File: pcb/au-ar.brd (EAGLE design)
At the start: 65 x 45 mm, 44 parts, among them U1 TPD12S520DBTR, U2 TPD12S521DBTR

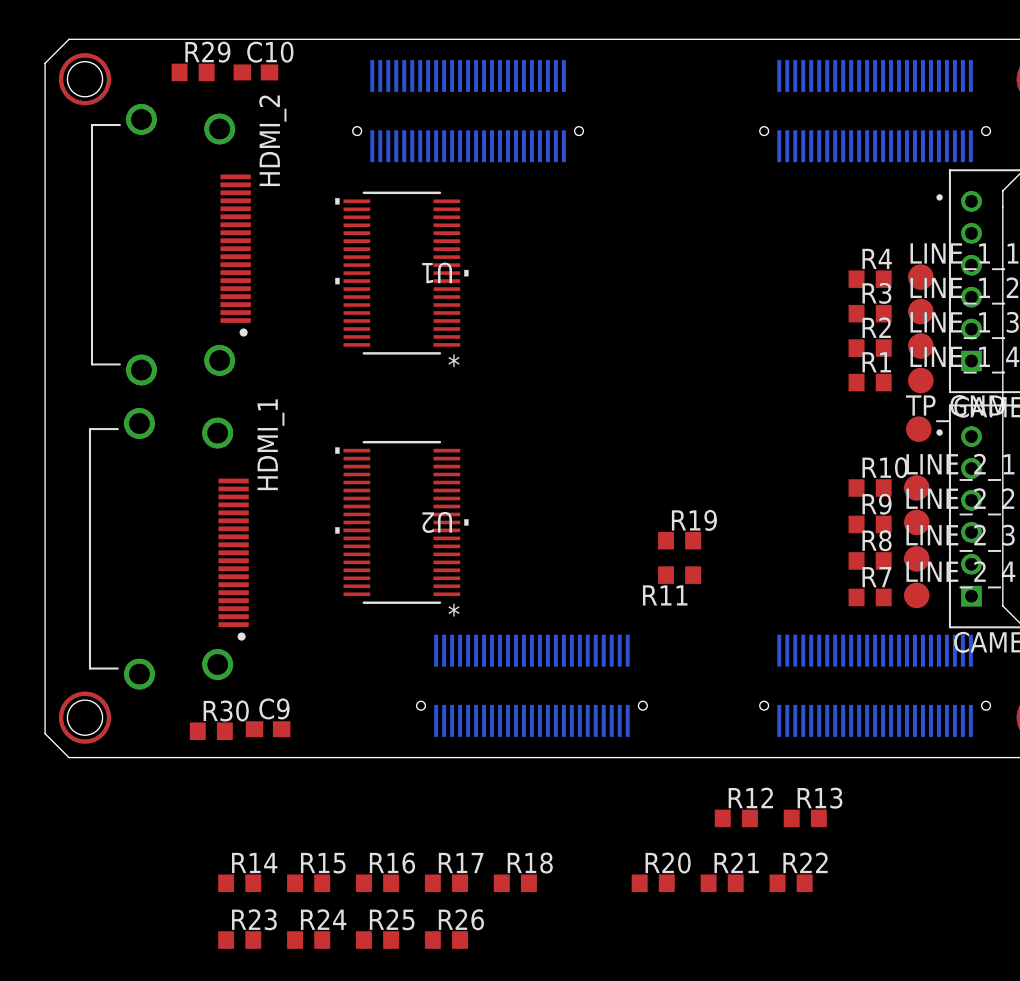
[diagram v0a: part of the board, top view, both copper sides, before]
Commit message: placed signal config resistors for camera trigger interface. relocated hdmi ports
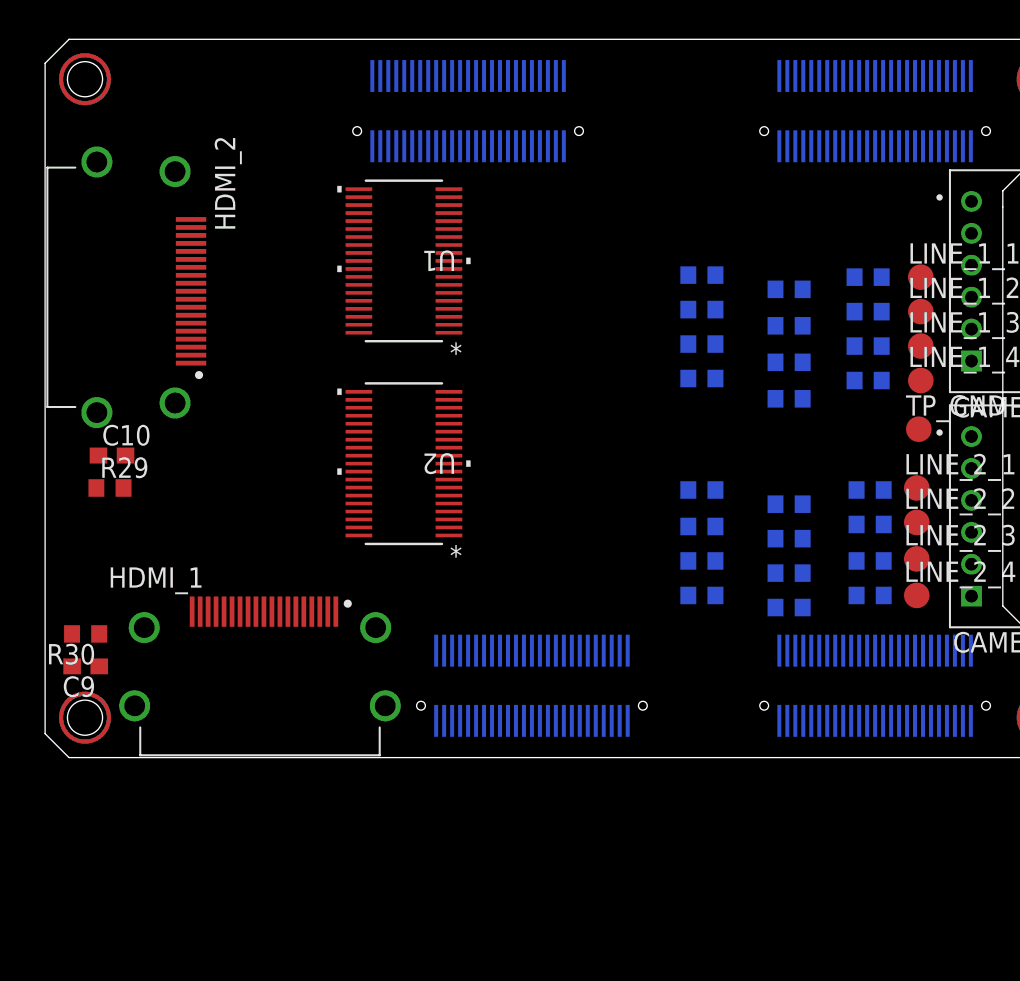
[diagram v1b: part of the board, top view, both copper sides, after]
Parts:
- moved R14 50.7 mm to (46.6, 29.3), flipped to the bottom
- moved R22 38.5 mm to (41.1, 30.2), flipped to the bottom, turned to 180 degrees
- moved R23 36.1 mm to (41.1, 10.2), flipped to the bottom, turned to 180 degrees
- moved R21 36.0 mm to (41.1, 28.1), flipped to the bottom, turned to 180 degrees
- moved R15 34.7 mm to (46.6, 9.40), flipped to the bottom
- moved R24 34.2 mm to (41.1, 12.3), flipped to the bottom, turned to 180 degrees
- moved R20 33.9 mm to (41.1, 25.9), flipped to the bottom, turned to 180 degrees
- moved R25 32.9 mm to (41.1, 14.5), flipped to the bottom, turned to 180 degrees
- moved R26 32.4 mm to (41.1, 16.8), flipped to the bottom, turned to 180 degrees
- moved R16 32.3 mm to (46.6, 11.6), flipped to the bottom
- moved R13 30.9 mm to (46.6, 27.1), flipped to the bottom
- moved R17 30.4 mm to (46.6, 13.7), flipped to the bottom
- moved R18 29.3 mm to (46.6, 15.9), flipped to the bottom
- moved R12 28.8 mm to (46.6, 24.8), flipped to the bottom
- moved R29 26.6 mm to (4.06, 16.9)
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
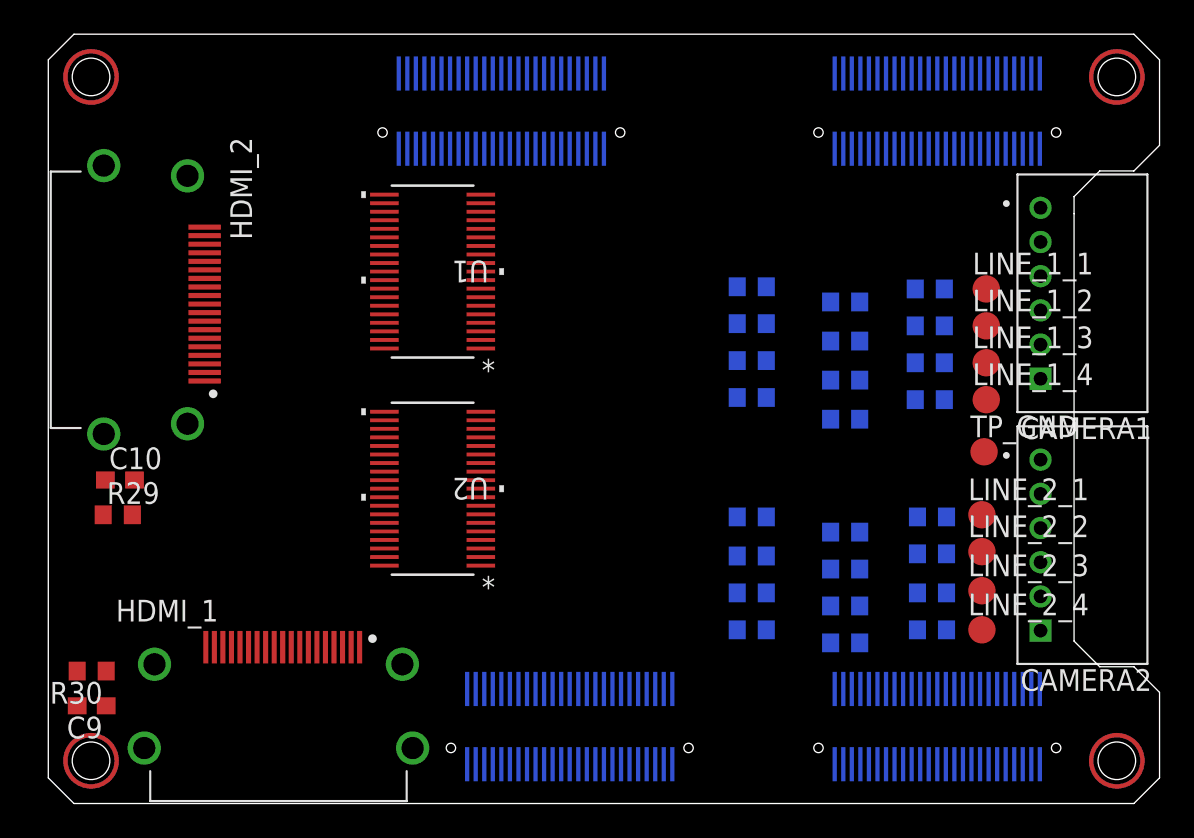
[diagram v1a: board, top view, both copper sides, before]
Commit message: rearranged hdmi ports. removed end mounting holes to make room for dual ports on the end. added footprint for spi flash and added to schematic.
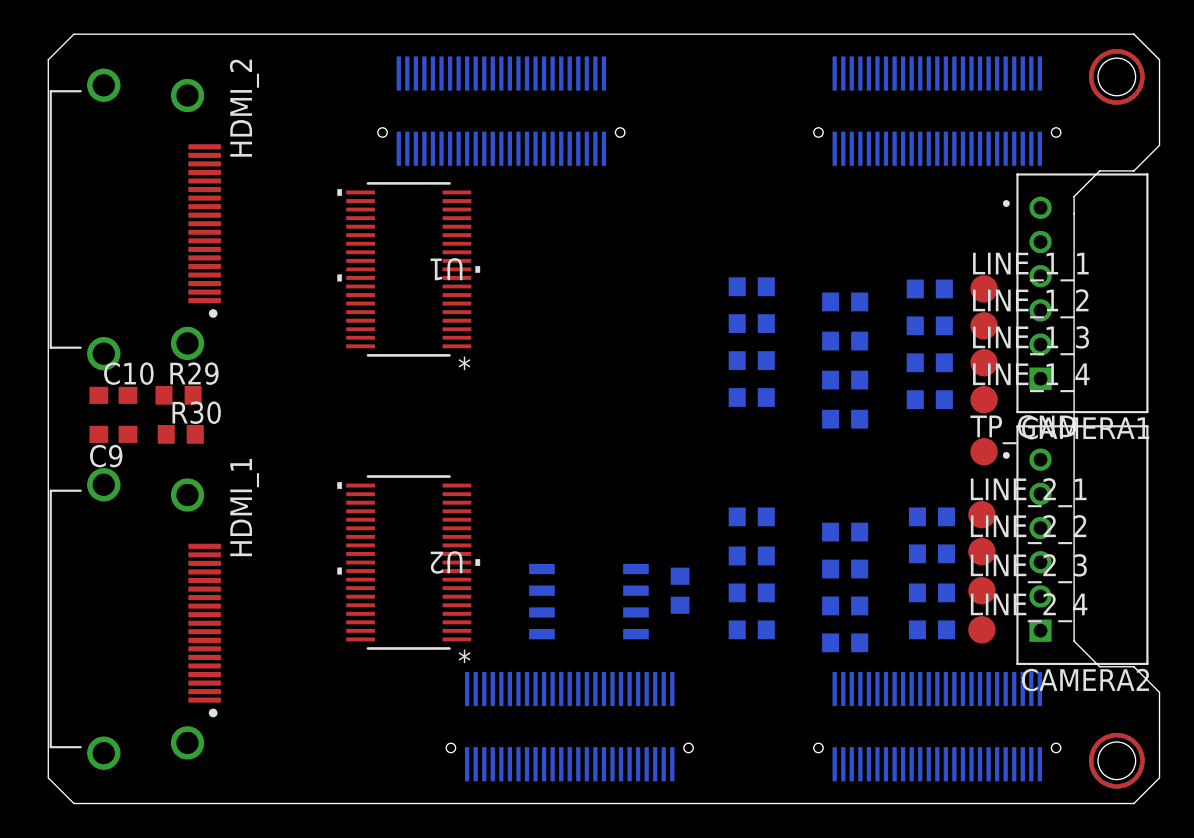
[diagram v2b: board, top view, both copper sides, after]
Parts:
- added R5: 47k, rcl:R0603
- added U$1: W25Q80DVSNIG, TDP12S521:SOIC8
- moved C9 15.9 mm to (3.81, 21.6)
- moved R30 14.8 mm to (7.75, 21.6), turned to 0 degrees
- moved R29 7.84 mm to (7.62, 23.9)
- moved C10 4.97 mm to (3.81, 23.9)
- moved HDMI_2 4.70 mm to (9.14, 34.2)
- moved HDMI_1 4.62 mm to (9.14, 10.8), turned to 270 degrees
- moved U2 4.54 mm to (21.1, 14.1)
- moved U1 1.40 mm to (21.1, 31.2)
- moved LINE_1_1 0.13 mm to (54.7, 30.1)
- moved LINE_1_2 0.13 mm to (54.7, 27.9)
- moved LINE_1_3 0.13 mm to (54.7, 25.8)
- moved LINE_1_4 0.13 mm to (54.7, 23.6)
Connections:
- net N$11 renamed SCL1_FPGA
- net N$12 renamed SDA1_FPGA
- net N$15 renamed HP1_FPGA
- removed net N$16: U2.1
- removed net N$17: U2.2
- removed net N$2: B1.CB_1
- removed net N$40: U1.1
- removed net N$41: U1.2
- removed net N$42: U1.11, U1.14, U1.16, U1.3, U1.5, U1.8
- removed net N$43: U1.25, U1.28, U1.31, U1.34, U1.36, U1.37
- removed net PIN: B1.AB_1
- new net 5V: B1.AB_1, B1.AB_50, B1.BB_1, B1.BB_50, B1.CB_1, B1.CB_50, B1.DB_1, B1.DB_50, U1.1, U2.1
- new net HP2_FPGA: U1.19
- new net SCL2_FPGA: U1.17
- new net SDA2_FPGA: U1.18
- new net SPI_CLK: U$1.6
- new net SPI_DI: U$1.5
- new net SPI_DO: U$1.2
- net 3V3: now also B1.AB_13, B1.AB_19, B1.AB_25, B1.AB_26, B1.AB_32, B1.AB_38, B1.AB_44, B1.AB_7, B1.BB_13, B1.BB_19, B1.BB_25, B1.BB_26, B1.BB_32, B1.BB_38, B1.BB_44, B1.BB_7, B1.CB_13, B1.CB_19, B1.CB_25, B1.CB_26, B1.CB_32, B1.CB_38, B1.CB_44, B1.CB_7, B1.DB_13, B1.DB_19, B1.DB_25, B1.DB_26, B1.DB_32, B1.DB_38, B1.DB_44, B1.DB_7, R5.2, U$1.3, U$1.7, U$1.8, U1.2, U2.2
- net CLK1_N: now also B1.BB_34
- net CLK1_P: now also B1.BB_33
- net CLK2_N: now also B1.BB_40
- net CLK2_P: now also B1.BB_39
- net D01_N: now also B1.BB_17
- net D01_P: now also B1.BB_18
- net D02_N: now also B1.BB_11
- net D02_P: now also B1.BB_12
- net D11_N: now also B1.BB_31
- net D11_P: now also B1.BB_30
- net D12_N: now also B1.BB_37
- net D12_P: now also B1.BB_36
- net D21_N: now also B1.BB_20
- net D21_P: now also B1.BB_21
- net D22_N: now also B1.BB_14
- net D22_P: now also B1.BB_15
- net GND: now also B1.AB_10, B1.AB_16, B1.AB_22, B1.AB_29, B1.AB_35, B1.AB_4, B1.AB_41, B1.AB_47, B1.BB_10, B1.BB_16, B1.BB_22, B1.BB_29, B1.BB_35, B1.BB_4, B1.BB_41, B1.BB_47, B1.CB_10, B1.CB_16, B1.CB_22, B1.CB_29, B1.CB_35, B1.CB_4, B1.CB_41, B1.CB_47, B1.DB_10, B1.DB_16, B1.DB_22, B1.DB_29, B1.DB_35, B1.DB_4, B1.DB_41, B1.DB_47, U$1.4, U1.11, U1.14, U1.16, U1.25, U1.28, U1.3, U1.31, U1.34, U1.36, U1.37, U1.5, U1.8
- net LINE_1_1: now also B1.AB_24
- net LINE_1_2: now also B1.AB_21
- net LINE_1_3: now also B1.AB_18
- net LINE_1_4: now also B1.AB_15
- net LINE_2_1: now also B1.AB_12
- net LINE_2_2: now also B1.AB_9
- net LINE_2_3: now also B1.AB_6
- net LINE_2_4: now also B1.AB_3
- net N$1: now also R5.1, U$1.1; no longer B1.BB_1

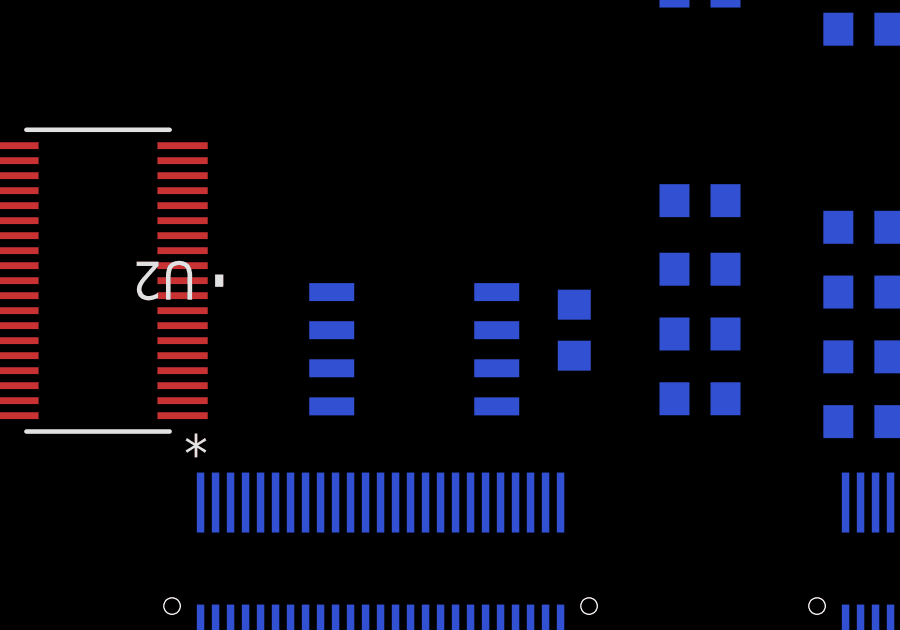
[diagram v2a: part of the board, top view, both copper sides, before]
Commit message: added remaining connections in schematic for spi flash and hdmi ddc bus
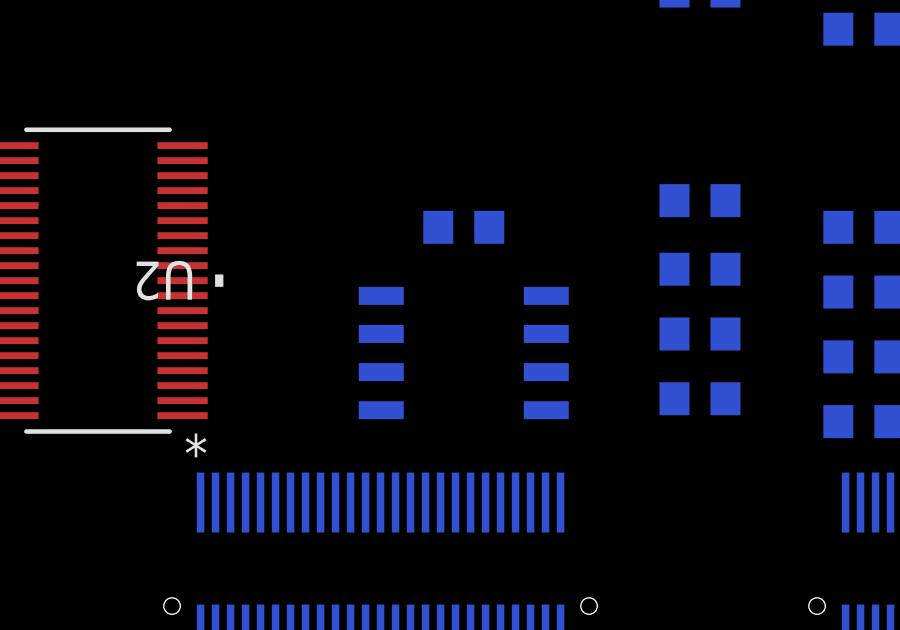
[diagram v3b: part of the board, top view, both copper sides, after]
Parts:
- moved R5 5.03 mm to (33.3, 15.9), turned to 0 degrees
- moved U$1 1.66 mm to (33.3, 11.7)
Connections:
- removed net N$1: R5.1, U$1.1
- new net EXT_CLK: B1.CB_45
- new net SCL3: B1.CB_9
- new net SDA3: B1.CB_12
- new net SPI_CS: B1.CB_27, R5.1, U$1.1
- net D01_N: now also B1.BB_31; no longer B1.BB_17
- net D01_P: now also B1.BB_30; no longer B1.BB_18
- net D11_N: now also B1.BB_20; no longer B1.BB_31
- net D11_P: now also B1.BB_21; no longer B1.BB_30
- net D21_N: now also B1.BB_28; no longer B1.BB_20
- net D21_P: now also B1.BB_27; no longer B1.BB_21
- net HP1_FPGA: now also B1.CB_48
- net HP2_FPGA: now also B1.AB_48
- net SCL1_FPGA: now also B1.CB_39
- net SCL2_FPGA: now also B1.AB_42
- net SDA1_FPGA: now also B1.CB_42
- net SDA2_FPGA: now also B1.AB_45
- net SPI_CLK: now also B1.CB_36
- net SPI_DI: now also B1.CB_33
- net SPI_DO: now also B1.CB_30

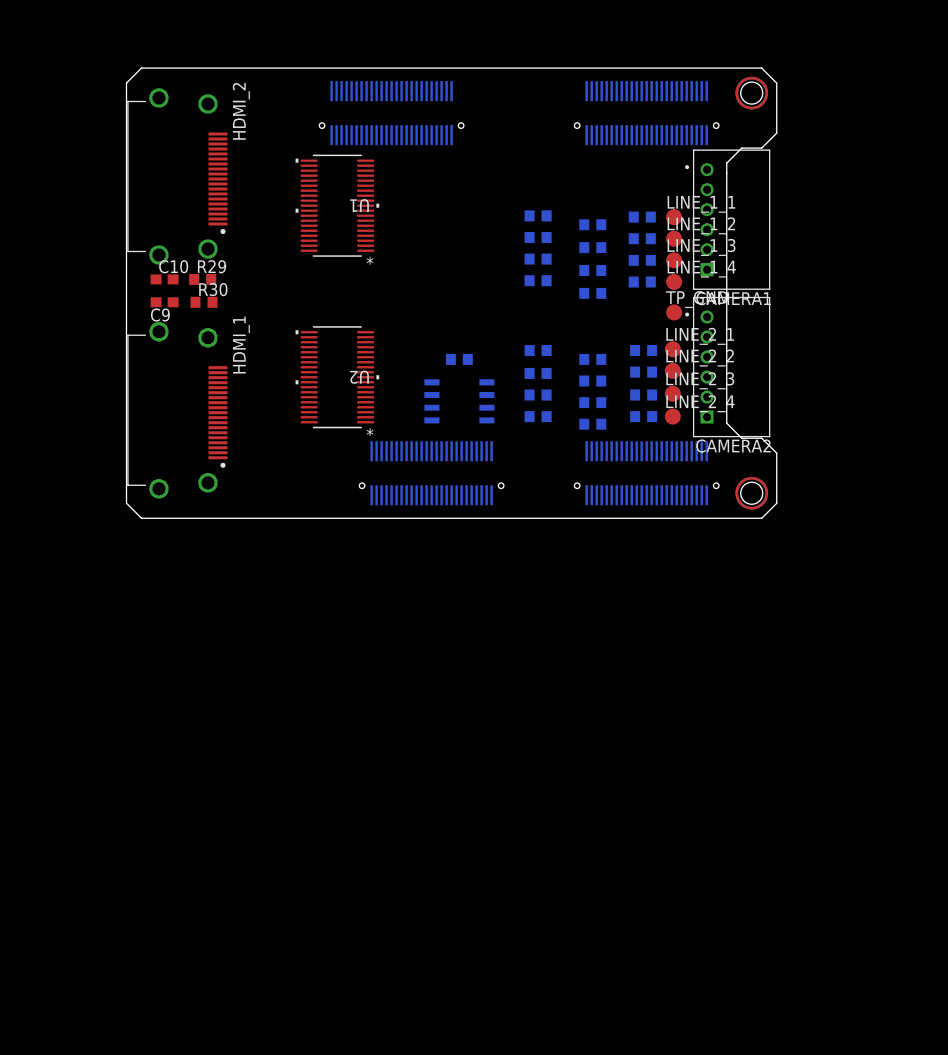
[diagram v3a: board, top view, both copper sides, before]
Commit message: started routing hdmi tmds signals. had to make min hole size .2mm
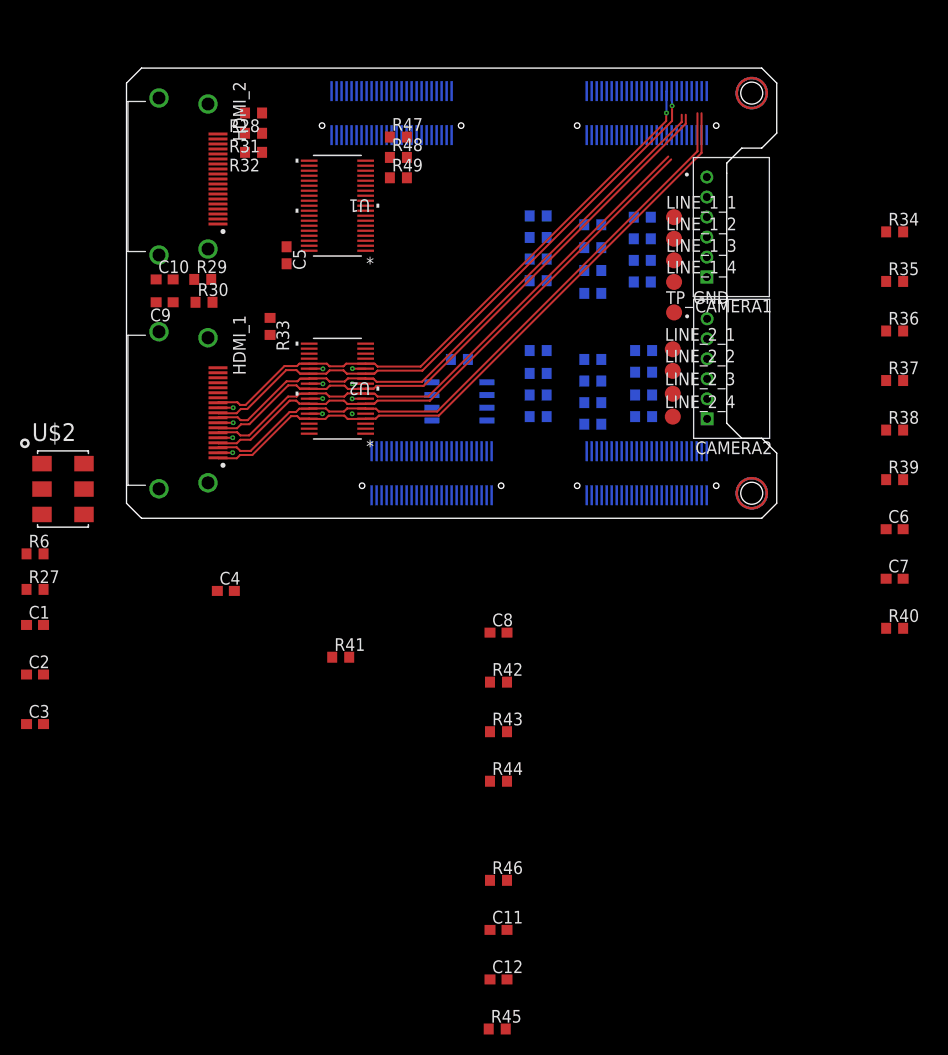
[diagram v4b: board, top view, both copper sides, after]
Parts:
- added C1: 1uF, rcl:C0603
- added C11, C12, C2, C3, C4, C5, C6, C7, C8: 0.1uF, rcl:C0603
- added R27, R6: 3k, rcl:R0603
- added R28, R37: 1k, rcl:R0603
- added R31, R32, R33, R34, R43, R44, R46, R47, R48, R49: 47k, rcl:R0603
- added R35: NP, rcl:R0603
- added R36, R40, R41: 10k, rcl:R0603
- added R38, R39: 27k, rcl:R0603
- added R42, R45: 100k, rcl:R0603
- added U$2: SI514, lupa300-components:XTAL-6PIN
- C10, C9: value 1uF -> 0.1uF
- moved U2 1.14 mm to (21.1, 13.0)
- moved CAMERA1 0.74 mm to (58.0, 29.1)
- moved CAMERA2 0.18 mm to (58.0, 14.9)
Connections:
- removed net N$55: U2.11, U2.14, U2.3, U2.5, U2.8
- removed net N$56: U2.25, U2.28, U2.31, U2.34, U2.36, U2.37
- new net CEC1: HDMI_1.13, R39.2, U2.23
- new net CEC1_FPGA: B1.CB_3, R43.1, U2.16
- new net CEC2: HDMI_2.13, R38.2, U1.23
- new net CEC2_FPGA: B1.AB_39, R49.1, U1.16
- new net N$1: C5.1, U1.37
- new net N$11: HDMI_1.14, R36.2
- new net N$12: C3.1, R41.1, U1.2
- new net N$15: C7.1, R40.1, U2.2
- new net N$16: C8.1, U2.37
- new net N$2: HDMI_2.14, R35.2
- net 3V3: now also C1.1, C2.1, R27.2, R38.1, R39.1, R40.2, R41.2, R42.2, R43.2, R44.2, R45.2, R46.2, R47.2, R48.2, R49.2, R6.2, U$2.P$6; no longer U1.2, U2.2
- net 5V: now also C4.1, C6.1, R31.1, R32.1, R33.1, R34.1
- net 5VHDMI1: now also C11.1, R37.1
- net 5VHDMI2: now also C12.1, R28.1
- net EXT_CLK: now also U$2.P$4
- net GND: now also C1.2, C11.2, C12.2, C2.2, C3.2, C4.2, C5.2, C6.2, C7.2, C8.2, R35.1, R36.1, U$2.P$3, U2.11, U2.14, U2.25, U2.28, U2.3, U2.31, U2.34, U2.36, U2.5, U2.8; no longer U1.16, U1.37
- net HP1: now also R37.2
- net HP1_FPGA: now also R42.1
- net HP2: now also R28.2
- net HP2_FPGA: now also R45.1
- net SCL1: now also R33.2
- net SCL1_FPGA: now also R44.1
- net SCL2: now also R31.2
- net SCL2_FPGA: now also R48.1
- net SCL3: now also R27.1, U$2.P$2
- net SDA1: now also R34.2
- net SDA1_FPGA: now also R46.1
- net SDA2: now also R32.2
- net SDA2_FPGA: now also R47.1
- net SDA3: now also B1.CB_6, R6.1, U$2.P$1; no longer B1.CB_12
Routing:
- net D21_P: track 0.00 -> 65.5 mm
- net D21_N: track 0.00 -> 64.8 mm
- net CLK1_P: track 0.00 -> 61.1 mm, vias 0 -> 1
- net D01_P: track 0.00 -> 60.9 mm
- net CLK1_N: track 0.00 -> 60.2 mm, vias 0 -> 1
- net D01_N: track 0.00 -> 60.1 mm
- net D11_P: track 0.00 -> 57.6 mm
- net D11_N: track 0.00 -> 57.2 mm
- net GND: track 0.00 -> 15.5 mm, vias 0 -> 12
- added copper zone on layer 2, net GND

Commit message: more routing
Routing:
- net D21_P: track 65.5 -> 24.4 mm
- net D21_N: track 64.8 -> 24.2 mm
- net CLK1_P: track 61.1 -> 22.8 mm, vias 1 -> 0
- net D01_P: track 60.9 -> 22.9 mm
- net CLK1_N: track 60.2 -> 22.5 mm, vias 1 -> 0
- net D01_N: track 60.1 -> 22.7 mm
- net D11_P: track 57.6 -> 23.5 mm
- net D11_N: track 57.2 -> 23.3 mm
- net CLK2_P: track 0.00 -> 9.92 mm
- net D12_N: track 0.00 -> 9.90 mm
- net D22_N: track 0.00 -> 9.90 mm
- net D22_P: track 0.00 -> 9.90 mm
- net D02_P: track 0.00 -> 9.90 mm
- net CLK2_N: track 0.00 -> 9.89 mm
- net D02_N: track 0.00 -> 9.88 mm
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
